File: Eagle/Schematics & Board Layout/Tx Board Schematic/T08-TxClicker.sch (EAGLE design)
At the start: 76 parts, among them U1 CC430F513X---RGZ48, Y1 26MHz

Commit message: TX_Schematic Update
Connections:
- net P1.7: now also S4.2; no longer S1.2
- net P2.0: now also S3.2; no longer S2.2
- net P2.1: now also S2.2; no longer S3.2
- net P2.2: now also S1.2; no longer S4.2
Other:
- note added: "**Switches are alternate parts for resistive touch switch. DNI unless resistive touch switches fail to meet performance requirements. Resistive touch switch footprint will be incorperated into switch footprint**"
- moved on the sheet: S1, S2, S3, S4

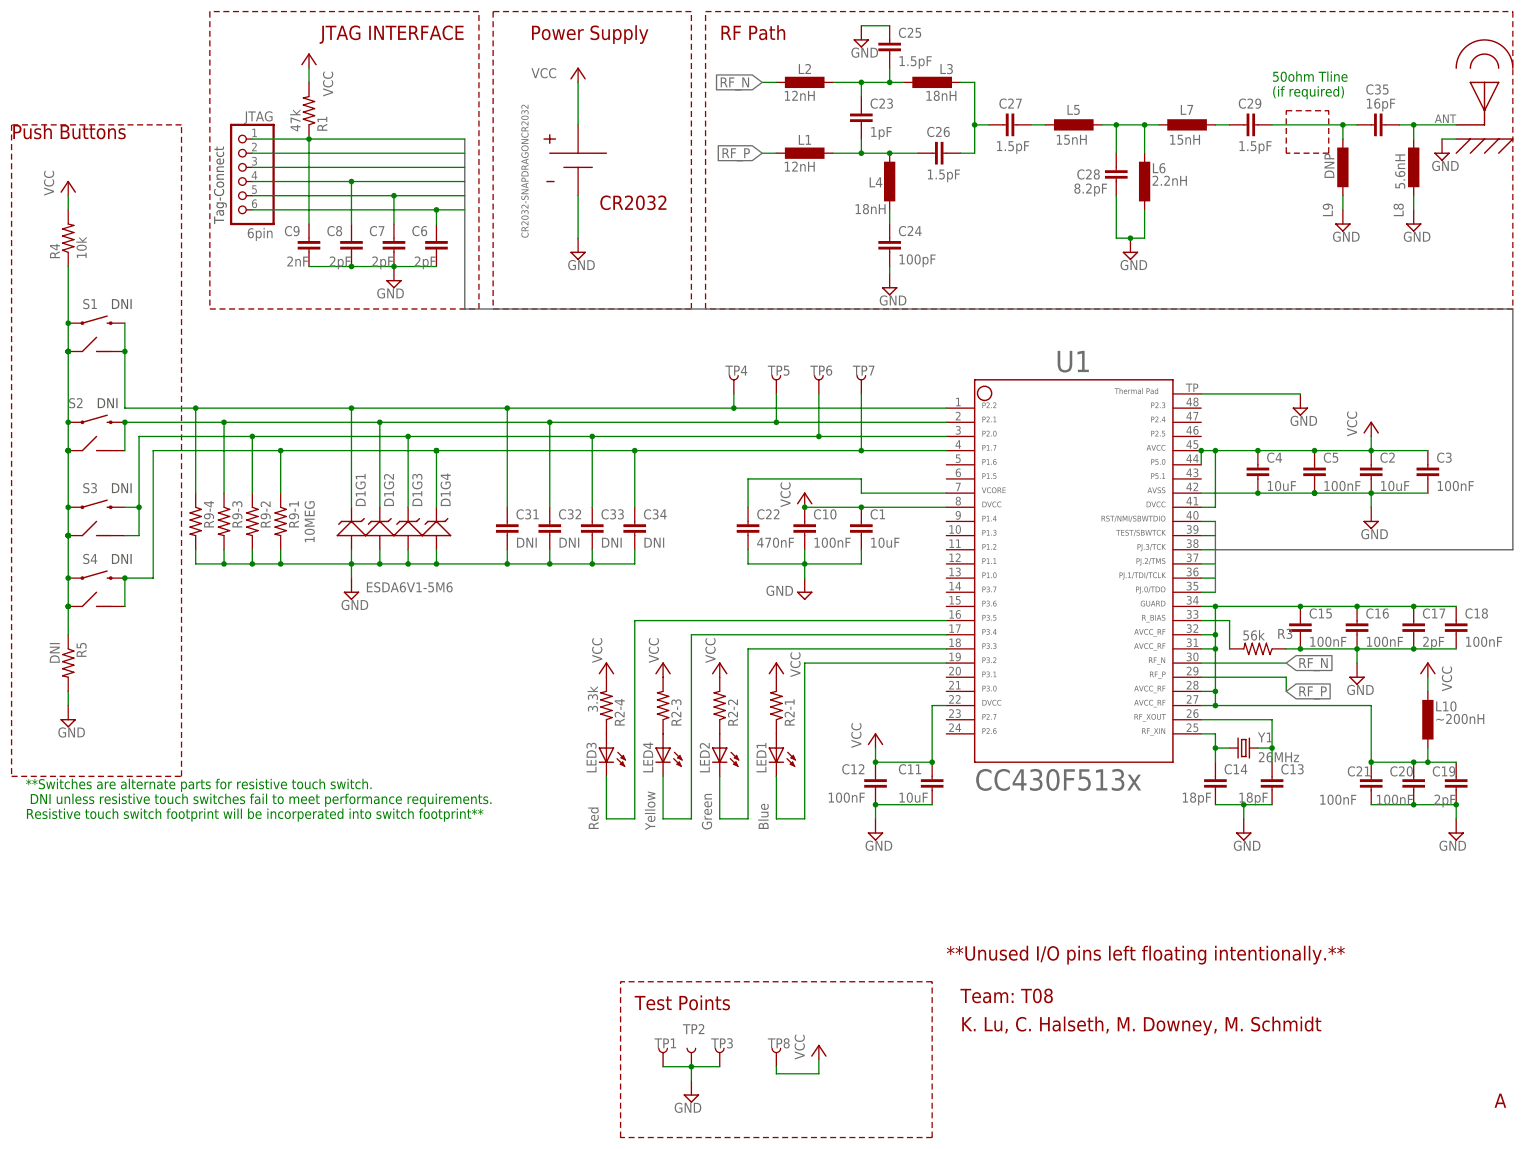
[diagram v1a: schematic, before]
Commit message: Added GPIO TP
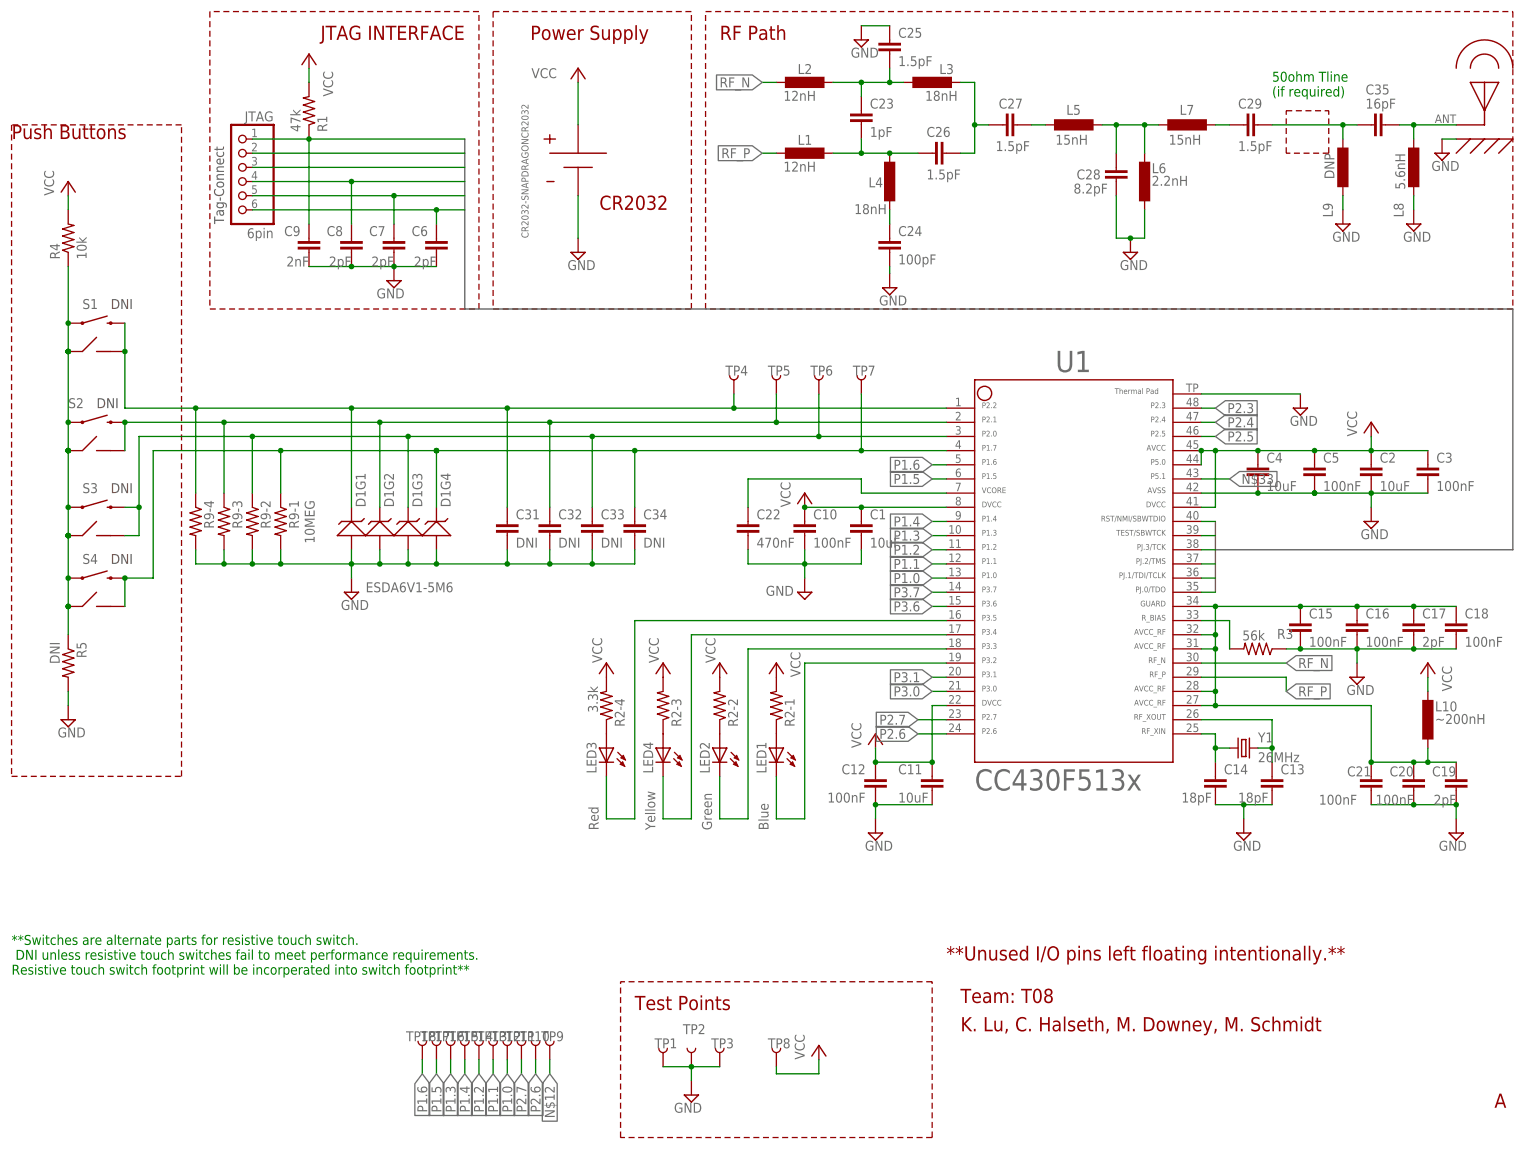
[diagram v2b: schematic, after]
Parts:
- added TP10, TP11, TP12, TP13, TP14, TP15, TP16, TP17, TP18, TP9: TEST-POINT3, SparkFun-Passives:TEST-POINT3
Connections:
- new net N$12: TP9.1
- new net N$33: U1.43
- new net P1.0: TP12.1, U1.13
- new net P1.1: TP13.1, U1.12
- new net P1.2: TP14.1, U1.11
- new net P1.3: TP16.1, U1.10
- new net P1.4: TP15.1, U1.9
- new net P1.5: TP17.1, U1.6
- new net P1.6: TP18.1, U1.5
- new net P2.3: U1.48
- new net P2.4: U1.47
- new net P2.5: U1.46
- new net P2.6: TP10.1, U1.24
- new net P2.7: TP11.1, U1.23
- new net P3.0: U1.21
- new net P3.1: U1.20
- new net P3.6: U1.15
- new net P3.7: U1.14
